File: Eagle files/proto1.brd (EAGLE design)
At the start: 100 x 80 mm, 10 parts, among them U1 RASPBERRY_PICOTH, U2 GY-521MPU6050, U3 HMC5883LGY-271, U4 ESP8266_ESP-01

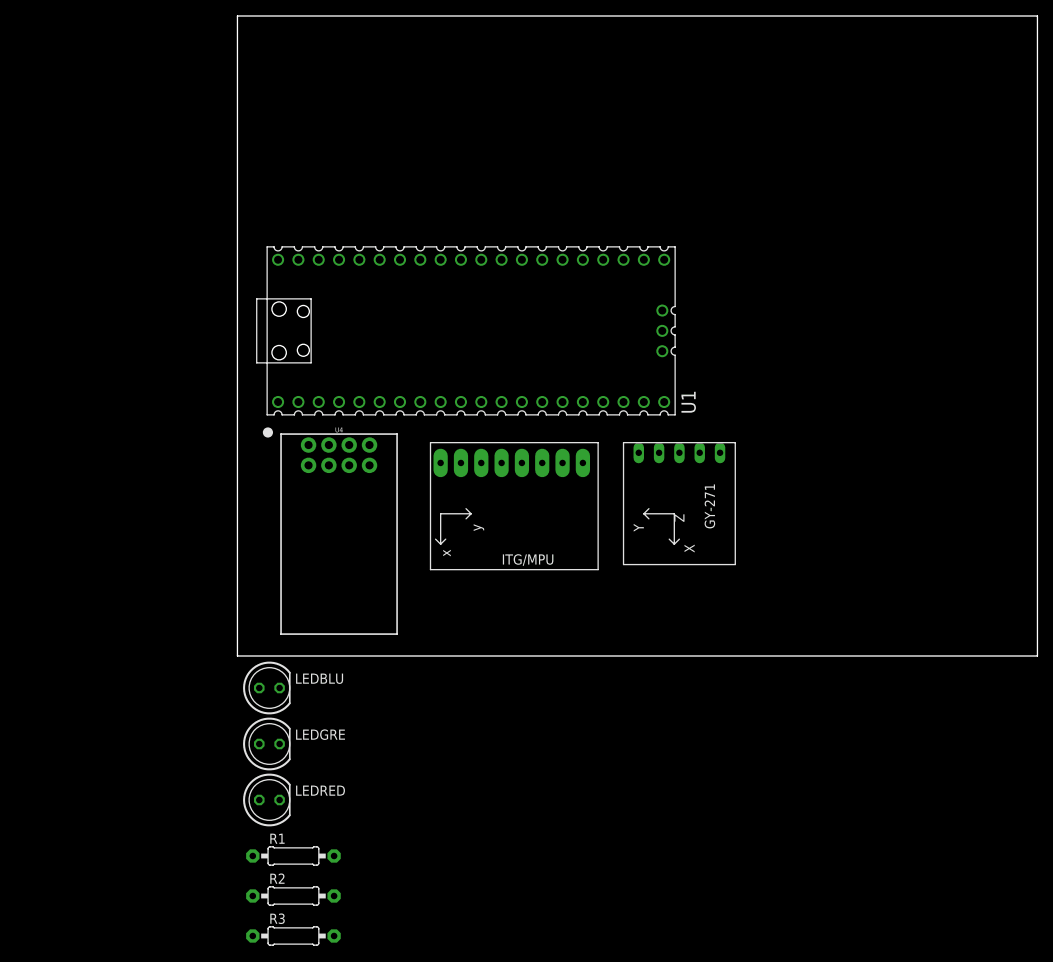
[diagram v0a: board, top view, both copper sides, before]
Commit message: Change microcontroller
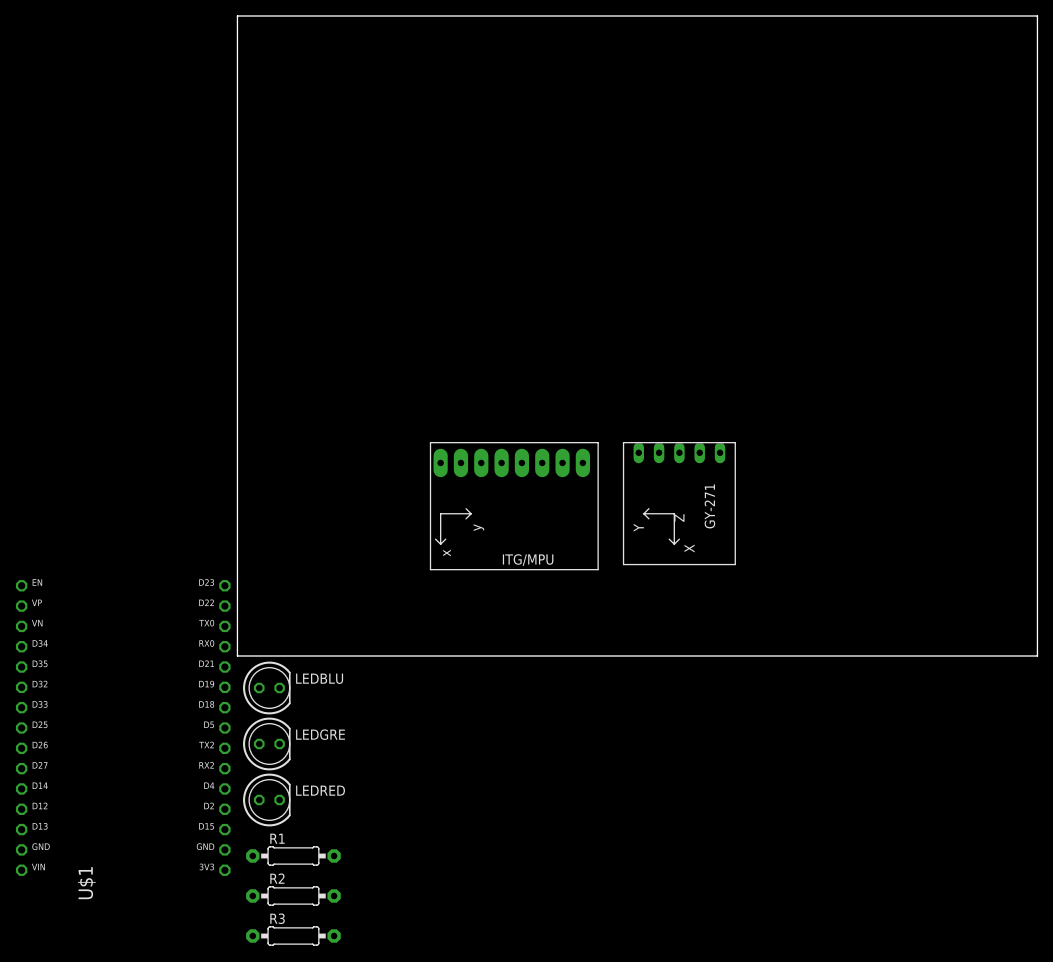
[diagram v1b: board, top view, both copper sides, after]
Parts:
- removed U1: RASPBERRY_PICOTH, RpiPico:PICO-PKG-TH
- removed U4: ESP8266_ESP-01, SparkFun-RF:ESP8266_ESP-01
- added U$1: ESP32_DEVKIT, DOIT_ESP32_DEVKIT:ESP32_DEVKIT
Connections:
- removed net N$2: U4.3
- removed net N$7: U4.7
- removed net RX: U1.2, U4.5
- removed net SWGND: U1.42
- removed net TX: U1.1, U4.1
- removed net VBUS: U1.40
- removed net VSYS: U1.39
- net GND: no longer U1.13, U1.18, U1.23, U1.28, U1.3, U1.33, U1.38, U1.8, U4.6, U4.8
- net LEDBLU: no longer U1.16
- net LEDGRE: no longer U1.14
- net LEDRED: no longer U1.15
- net SCL: no longer U1.7
- net SDA: no longer U1.6
- net VCC: no longer U1.36, U4.2, U4.4
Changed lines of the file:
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@@
 </autorouter>
 <elements>
-<element name="U1" library="RpiPico" package="PICO-PKG-TH" value="RASPBERRY_PICOTH" x="29.21" y="40.64" smashed="yes" rot="R90">
-<attribute name="NAME" x="57.277" y="30.226" size="1.778" layer="25" rot="R90"/>
-<attribute name="VALUE" x="48.895" y="44.196" size="1.778" layer="27" rot="R180"/>
-</element>
 <element name="U2" library="gy-521" package="GY-521" value="GY-521MPU6050" x="34.29" y="15.24" smashed="yes" rot="R270"/>
 <element name="U3" library="hmc5883l" package="GY-271" value="HMC5883LGY-271" x="54.61" y="19.05" smashed="yes" rot="R270"/>
-<element name="U4" library="SparkFun-RF" package="ESP8266_ESP-01" value="ESP8266_ESP-01" x="12.7" y="15.24" smashed="yes" rot="R180">
-<attribute name="NAME" x="12.7048" y="27.9536" size="0.6096" layer="25" ratio="20" rot="R180" align="top-center"/>
-<attribute name="SF_ID" value="WRL-13678" x="-33.02" y="29.21" size="1.778" layer="27" rot="R180" display="off"/>
-<attribute name="VALUE" x="12.7" y="8.89" size="0.6096" layer="27" ratio="20" rot="R180" align="center"/>
-</element>
 <element name="LEDBLU" library="led" library_urn="urn:adsk.eagle:library:259" package="LED5MM" package3d_urn="urn:adsk.eagle:package:15799/2" value="" x="4" y="-4" smashed="yes">
 <attribute name="NAME" x="7.175" y="-3.4666" size="1.27" layer="25" ratio="10"/>
@@
 <attribute name="VALUE" x="4.7394" y="-35.635" size="1.27" layer="27" ratio="10"/>
 </element>
+<element name="U$1" library="DOIT_ESP32_DEVKIT" package="ESP32_DEVKIT" value="ESP32_DEVKIT" x="-13" y="-9" smashed="yes">
+<attribute name="NAME" x="-18.08" y="-30.59" size="1.778" layer="25" rot="R90"/>
+<attribute name="VALUE" x="-9.19" y="-30.59" size="1.778" layer="27" rot="R90"/>
+</element>
 </elements>
 <signals>
-<signal name="VSYS">
-<contactref element="U1" pad="39"/>
-</signal>
-<signal name="VBUS">
-<contactref element="U1" pad="40"/>
-</signal>
-<signal name="SWGND">
-<contactref element="U1" pad="42"/>
-</signal>
 <signal name="GND">
 <contactref element="U2" pad="GND"/>
 <contactref element="U3" pad="GND"/>
-<contactref element="U1" pad="3"/>
-<contactref element="U1" pad="8"/>
-<contactref element="U1" pad="13"/>
-<contactref element="U1" pad="18"/>
-<contactref element="U1" pad="23"/>
-<contactref element="U1" pad="28"/>
-<contactref element="U1" pad="33"/>
-<contactref element="U1" pad="38"/>
-<contactref element="U4" pad="8"/>
-<contactref element="U4" pad="6"/>
-<wire x1="35.56" y1="49.53" x2="48.26" y2="49.53" width="0" layer="19" extent="1-1"/>
-<wire x1="22.86" y1="49.53" x2="35.56" y2="49.53" width="0" layer="19" extent="1-1"/>
-<wire x1="10.16" y1="49.53" x2="22.86" y2="49.53" width="0" layer="19" extent="1-1"/>
-<wire x1="48.26" y1="31.75" x2="48.26" y2="49.53" width="0" layer="19" extent="1-1"/>
-<wire x1="40.64" y1="24.13" x2="48.26" y2="31.75" width="0" layer="19" extent="1-1"/>
-<wire x1="35.56" y1="31.75" x2="40.64" y2="24.13" width="0" layer="19" extent="1-1"/>
-<wire x1="57.785" y1="25.4" x2="48.26" y2="31.75" width="0" layer="19" extent="1-1"/>
-<wire x1="22.86" y1="31.75" x2="35.56" y2="31.75" width="0" layer="19" extent="1-1"/>
-<wire x1="16.51" y1="23.83" x2="22.86" y2="31.75" width="0" layer="19" extent="1-1"/>
-<wire x1="11.43" y1="23.83" x2="16.51" y2="23.83" width="0" layer="19" extent="1-1"/>
-<wire x1="10.16" y1="31.75" x2="11.43" y2="23.83" width="0" layer="19" extent="1-1"/>
+<wire x1="40.64" y1="24.13" x2="57.785" y2="25.4" width="0" layer="19" extent="1-1"/>
 </signal>
 <signal name="SCL">
 <contactref element="U2" pad="SCL"/>
-<contactref element="U1" pad="7"/>
-<wire x1="20.32" y1="31.75" x2="38.1" y2="24.13" width="0" layer="19" extent="1-1"/>
 </signal>
 <signal name="SDA">
 <contactref element="U2" pad="SDA"/>
-<contactref element="U1" pad="6"/>
-<wire x1="17.78" y1="31.75" x2="35.56" y2="24.13" width="0" layer="19" extent="1-1"/>
 </signal>
 <signal name="N$5">
@@
 </signal>
 <signal name="VCC">
-<contactref element="U1" pad="36"/>
 <contactref element="U2" pad="VCC"/>
 <contactref element="U3" pad="VCC"/>
-<contactref element="U4" pad="4"/>
-<contactref element="U4" pad="2"/>
 <contactref element="LEDRED" pad="A"/>
 <contactref element="LEDBLU" pad="A"/>
 <contactref element="LEDGRE" pad="A"/>
 <wire x1="43.18" y1="24.13" x2="60.325" y2="25.4" width="0" layer="19" extent="1-1"/>
-<wire x1="13.97" y1="26.37" x2="43.18" y2="24.13" width="0" layer="19" extent="1-1"/>
-<wire x1="8.89" y1="26.37" x2="13.97" y2="26.37" width="0" layer="19" extent="1-1"/>
-<wire x1="15.24" y1="49.53" x2="13.97" y2="26.37" width="0" layer="19" extent="1-1"/>
-<wire x1="2.73" y1="-4" x2="8.89" y2="26.37" width="0" layer="19" extent="1-1"/>
+<wire x1="2.73" y1="-4" x2="43.18" y2="24.13" width="0" layer="19" extent="1-1"/>
 <wire x1="2.73" y1="-11" x2="2.73" y2="-4" width="0" layer="19" extent="1-1"/>
 <wire x1="2.73" y1="-18" x2="2.73" y2="-11" width="0" layer="19" extent="1-1"/>
@@
 <contactref element="U3" pad="SDA"/>
 </signal>
-<signal name="N$2">
-<contactref element="U4" pad="3"/>
-</signal>
-<signal name="N$7">
-<contactref element="U4" pad="7"/>
-</signal>
-<signal name="TX">
-<contactref element="U1" pad="1"/>
-<contactref element="U4" pad="1"/>
-<wire x1="5.08" y1="31.75" x2="16.51" y2="26.37" width="0" layer="19" extent="1-1"/>
-</signal>
-<signal name="RX">
-<contactref element="U1" pad="2"/>
-<contactref element="U4" pad="5"/>
-<wire x1="7.62" y1="31.75" x2="8.89" y2="23.83" width="0" layer="19" extent="1-1"/>
-</signal>
 <signal name="LEDGRE">
-<contactref element="U1" pad="14"/>
 <contactref element="R3" pad="1"/>
-<wire x1="1.92" y1="-35" x2="38.1" y2="31.75" width="0" layer="19" extent="1-1"/>
 </signal>
 <signal name="LEDRED">
-<contactref element="U1" pad="15"/>
 <contactref element="R1" pad="1"/>
-<wire x1="1.92" y1="-25" x2="40.64" y2="31.75" width="0" layer="19" extent="1-1"/>
 </signal>
 <signal name="LEDBLU">
-<contactref element="U1" pad="16"/>
 <contactref element="R2" pad="1"/>
-<wire x1="1.92" y1="-30" x2="43.18" y2="31.75" width="0" layer="19" extent="1-1"/>
 </signal>
 <signal name="N$1">
